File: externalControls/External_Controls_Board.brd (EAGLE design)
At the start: 109.9 x 48.2 mm, 23 parts

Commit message: Rev1 Functional
updated to Rev1 specifications
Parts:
- removed DYNA1, DYNA2: DYNAMIXEL-1X03HORIZ, MRDT-2015-Arm:MLX-SPOX5268-3PIN
- removed FET_DYNA1, FET_DYNA2, FET_DYNA3, FET_DYNA4, FET_DYNA5, FET_DYNA6: BUK9Y4R4-40EPOWER-SO8, MRDT-2015-General:POWER-SO8
- removed LT1910CAP-DYNA1, LT1910CAP-DYNA2: .1µF, resistor:C1206
- removed SV1: (no value), con-lsta:FE09W
- removed SV2, SV3: (no value), con-lsta:FE06W
- removed U$4: LT1910, MRDT-2015-PowerBoard:SO8
- removed U$7: MOUNTING_HOLE#8, MRDT-Hardware:#8_SCREW
- removed XB2: XBEE, maxstream:XBEE
- removed ZENER_DYNA1, ZENER_DYNA2: SMAJ5920, SparkFun-DiscreteSemi:SMA-DIODE
- added U$8: MOLEX7-PIN, logicShifter:MOLEX7PIN
- U$1: value LT1910 -> 74AHCT125; device MRDT-2015-PowerBoard:SO8 -> logicShifter:DIP16
- moved U$5 68.3 mm to (95.4, 21.6)
- moved U$6 45.4 mm to (82.5, 52.0)
- moved U$3 23.5 mm to (27.4, 13.8)
- moved U$1 8.43 mm to (100.6, 32.8), turned to 180 degrees
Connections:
- removed net 5V: FET_DYNA3.5, FET_DYNA3.6, FET_DYNA3.7, FET_DYNA3.8, FET_DYNA4.5, FET_DYNA4.6, FET_DYNA4.7, FET_DYNA4.8, FET_DYNA5.5, FET_DYNA5.6, FET_DYNA5.7, FET_DYNA5.8, FET_DYNA6.5, FET_DYNA6.6, FET_DYNA6.7, FET_DYNA6.8
- removed net CAM_12V: SV1.9, SV2.1
- removed net CAM_GND: SV1.8, SV2.2
- removed net CAM_PWM0: SV1.1, SV2.6
- removed net CAM_PWM1: SV1.2, SV2.5
- removed net CAM_PWM2: SV1.3, SV2.4
- removed net CAM_PWM3: SV1.4, SV2.3
- removed net CAM_VIDEO: SV1.7
- removed net CAM_VIDEO_GND: SV1.6
- removed net DYNA_ENABLE_1: U$2.PM4, U$4.4
- removed net DYNA_ENABLE_2: U$1.4, U$2.PM5
- removed net GATE-DYNA1: FET_DYNA1.4, U$4.5
- removed net GATE-DYNA2: FET_DYNA2.4, U$1.5
- removed net N: DYNA2.P$2, FET_DYNA2.1, FET_DYNA2.2, FET_DYNA2.3
- removed net NC: SV1.5
- removed net PWM0_OUT: SV3.1
- removed net PWM1_OUT: SV3.2
- removed net PWM2_OUT: SV3.3
- removed net PWM3_OUT: SV3.4
- removed net SOURCE-DYNA1: DYNA1.P$2, FET_DYNA1.1, FET_DYNA1.2, FET_DYNA1.3
- removed net VCC: XB2.1
- net +12V: now also U$8.2; no longer FET_DYNA1.5, FET_DYNA1.6, FET_DYNA1.7, FET_DYNA1.8, FET_DYNA2.5, FET_DYNA2.6, FET_DYNA2.7, FET_DYNA2.8, LT1910CAP-DYNA1.2, LT1910CAP-DYNA2.2, SV3.6, U$1.6, U$1.8, U$4.6, U$4.8
- net +5V: now also U$1.P$14
- net DYNA_DATA: now also U$8.3; no longer DYNA1.P$3, DYNA2.P$3, ZENER_DYNA1.C, ZENER_DYNA2.C
- net GND: now also U$1.P$1, U$1.P$10, U$1.P$13, U$1.P$4, U$1.P$7, U$8.PAD1; no longer DYNA1.P$1, DYNA2.P$1, LT1910CAP-DYNA1.1, LT1910CAP-DYNA2.1, SV3.5, U$1.1, U$4.1, XB2.10, ZENER_DYNA1.A, ZENER_DYNA2.A
- net N$1: now also U$1.P$3, U$8.7; no longer FET_DYNA3.1, FET_DYNA3.2, FET_DYNA3.3
- net N$2: now also U$1.P$6, U$8.6; no longer FET_DYNA4.1, FET_DYNA4.2, FET_DYNA4.3
- net N$3: now also U$1.P$8, U$8.5; no longer FET_DYNA5.1, FET_DYNA5.2, FET_DYNA5.3
- net N$4: now also U$1.P$11, U$8.4; no longer FET_DYNA6.1, FET_DYNA6.2, FET_DYNA6.3
- net TIVA_PWM0: now also U$1.P$2; no longer FET_DYNA3.4
- net TIVA_PWM1: now also U$1.P$5; no longer FET_DYNA4.4
- net TIVA_PWM2: now also U$1.P$9; no longer FET_DYNA5.4
- net TIVA_PWM3: now also U$1.P$12; no longer FET_DYNA6.4
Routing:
- net +5V: track 0.00 -> 99.3 mm, vias 0 -> 1
- net +12V: track 0.00 -> 87.6 mm
- net N$3: track 0.00 -> 36.3 mm, vias 0 -> 1
- net N$2: track 0.00 -> 34.0 mm
- net N$4: track 0.00 -> 30.1 mm, vias 0 -> 1
- net N$1: track 0.00 -> 26.6 mm
- net TIVA_PWM0: track 0.00 -> 26.6 mm, vias 0 -> 4
- net TIVA_PWM3: track 0.00 -> 25.6 mm, vias 0 -> 1
- net DYNA_DATA: track 0.00 -> 22.9 mm
- net TIVA_PWM2: track 0.00 -> 22.8 mm
- net TIVA_PWM1: track 0.00 -> 18.8 mm
- net GND: track 0.00 -> 11.2 mm
- added copper zone on layer 16, net GND
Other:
- board size 109.9 x 48.2 mm -> 89 x 48.2 mm

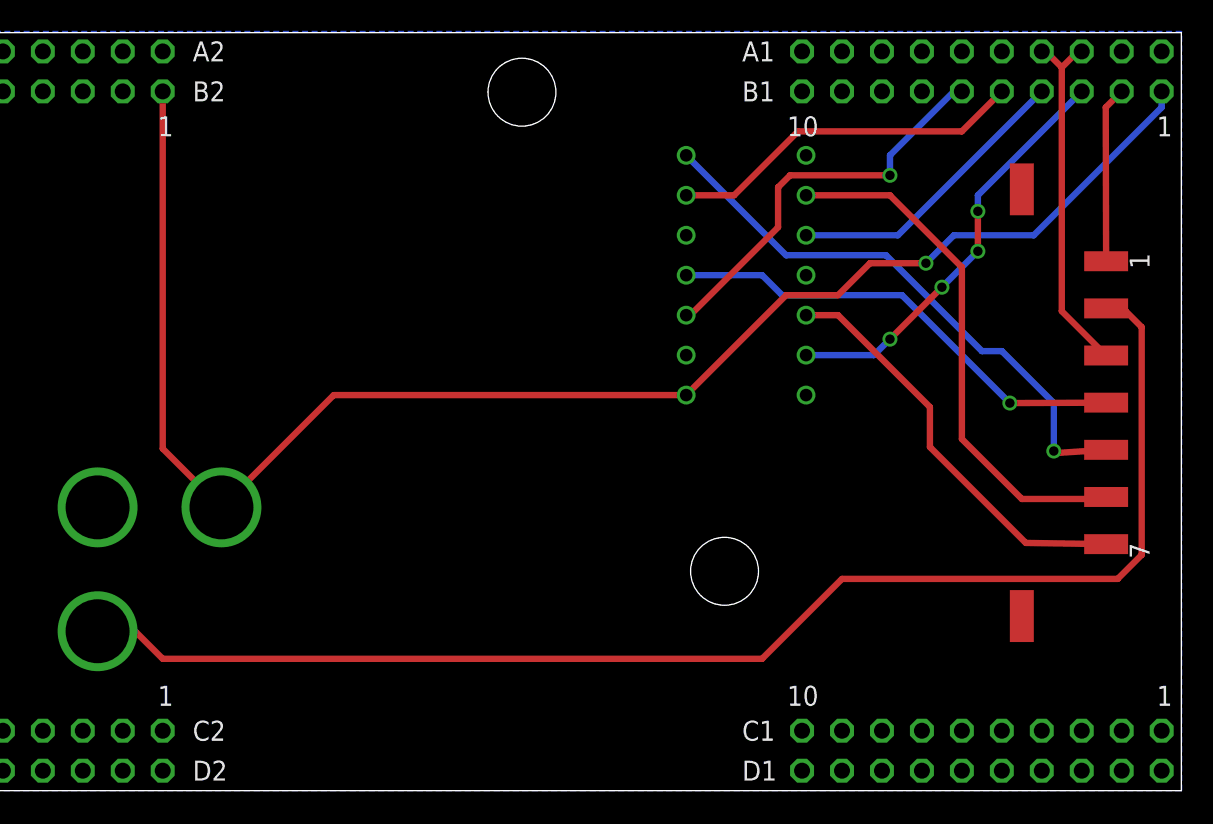
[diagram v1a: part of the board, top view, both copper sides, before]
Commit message: Updated Routing
optimized a few paths
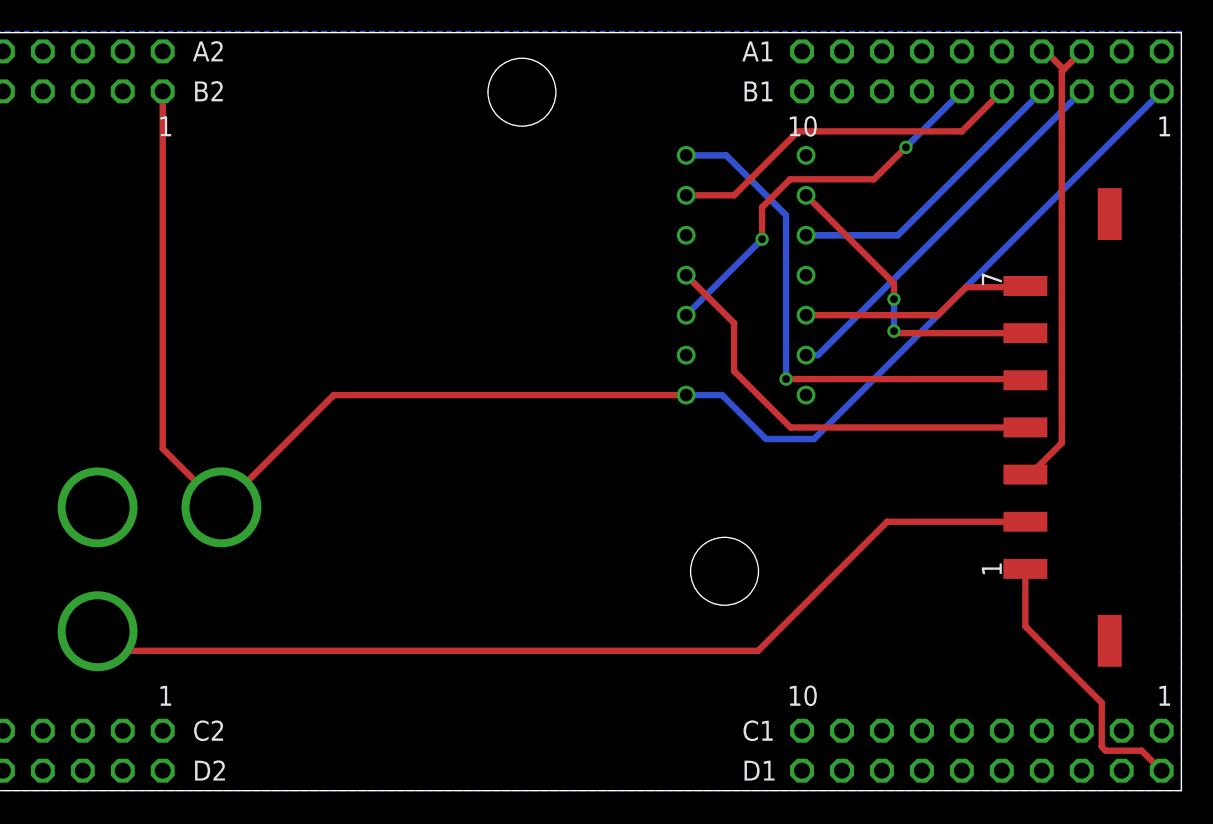
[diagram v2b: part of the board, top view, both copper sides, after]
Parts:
- moved U$8 32.8 mm to (120.7, 15.5), turned to 90 degrees
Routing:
- net +12V: track 87.6 -> 62.9 mm
- net N$2: track 34.0 -> 19.4 mm, vias 0 -> 2
- net N$1: track 26.6 -> 14.7 mm
- net DYNA_DATA: track 22.9 -> 30.4 mm
- net GND: track 11.2 -> 17.8 mm
- net N$3: track 36.3 -> 33.6 mm
- net N$4: track 30.1 -> 27.4 mm, vias 1 -> 0
- net TIVA_PWM0: track 26.6 -> 24.5 mm, vias 4 -> 0
- net +5V: track 99.3 -> 101.0 mm, vias 1 -> 0
- net TIVA_PWM3: track 25.6 -> 24.6 mm, vias 1 -> 2
